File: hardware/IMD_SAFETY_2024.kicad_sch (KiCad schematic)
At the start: 93 parts, among them J1 Main- M80-5300842, K2 TE AXICOM IM07DTS, Q1 2N7002, Q2 2N7002, SW1 Push Button, U1 LM393, U10 74HCS08, U13 74HC74, U14 LM393, U15 LM393, U16 LM393, U2 74AC04SC, U3 74LVC1G79, U6 74LVC1G79, U7 MC78M12CDTG, U8 LM1117IMP-5.0, U9 74HCS32

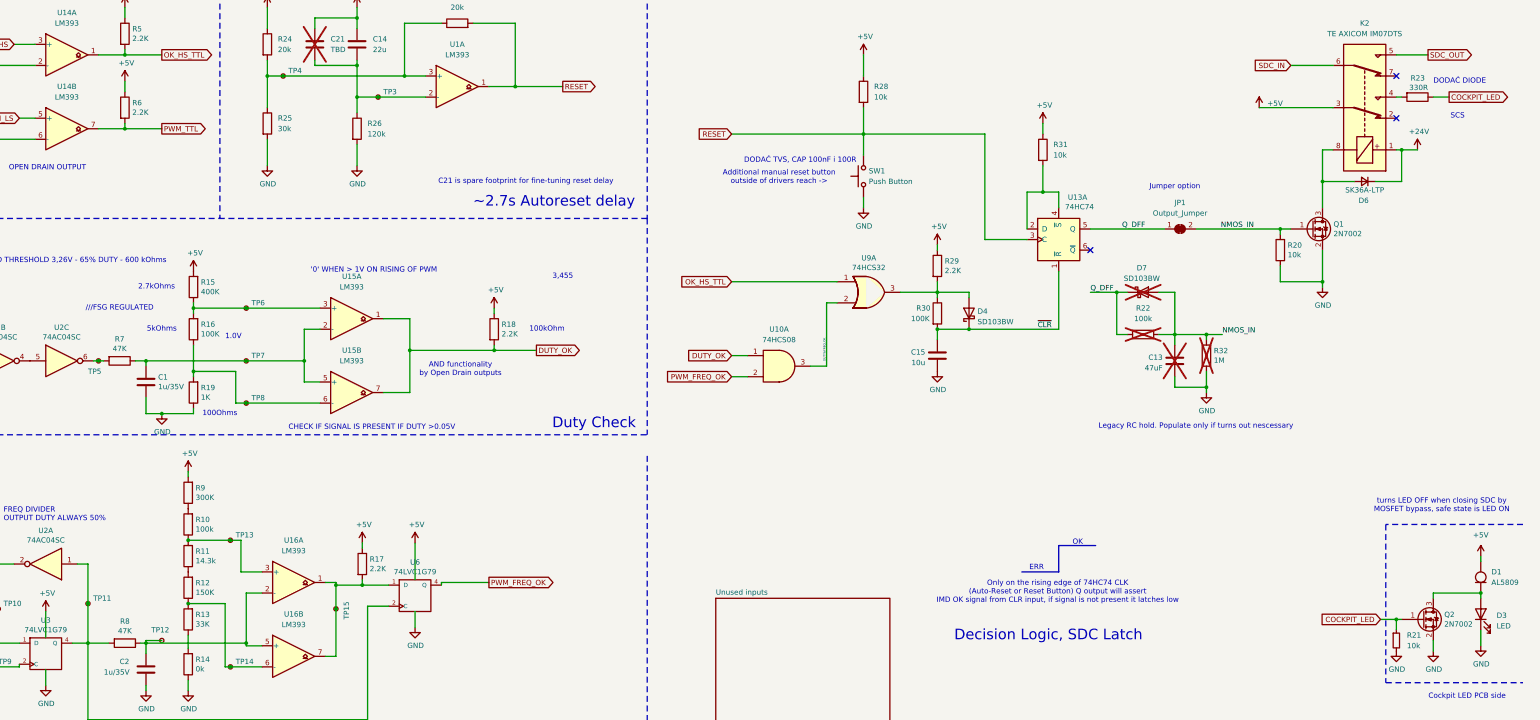
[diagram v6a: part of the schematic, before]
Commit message: Delete legacy RC hold, Add relay diode, Adjust Duty R Values via FSG tweaks TODO: RESET EMI Filter
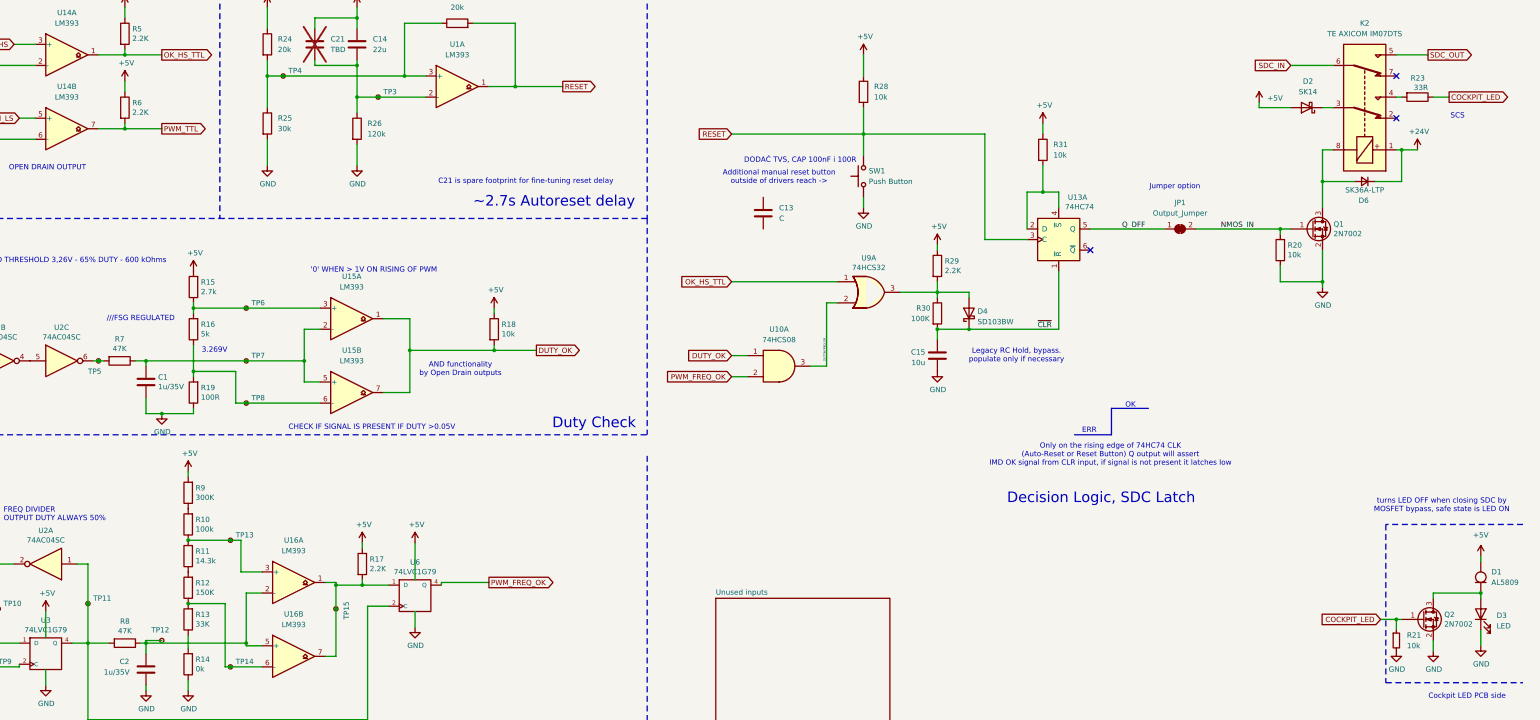
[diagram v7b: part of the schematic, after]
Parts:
- removed C13: 47uF, Capacitor_SMD:C_1206_3216Metric, symbol PUTM_EV_IMD_SAFETY_2021-rescue:C-Device
- removed D7: SD103BW, Diode_SMD:D_SOD-123F, symbol Device:D_Schottky
- removed R22: 100k, Resistor_SMD:R_0603_1608Metric, symbol PUTM_EV_IMD_SAFETY_2021-rescue:R-Device
- removed R32: 1M, Resistor_SMD:R_0603_1608Metric, symbol PUTM_EV_IMD_SAFETY_2021-rescue:R-Device
- added C13: C, symbol Device:C
- added D2: SK14, Diode_SMD:D_SMA, symbol Device:D_Schottky
- R15: value 400K -> 2.7k
- R16: value 100K -> 5k
- R18: value 2.2K -> 10k
- R19: value 1K -> 100R
- R23: value 330R -> 33R; footprint Resistor_SMD:R_0603_1608Metric -> Resistor_SMD:R_0805_2012Metric
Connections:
- net +5V: now also D2.2 (A); no longer K2.3
- new net: D2.1 (K), K2.3
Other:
- note added: "3.269V"
- note added: "Legacy RC Hold, bypass. populate only if necessary"
- note removed: "1.0V"
- note removed: "100Ohms"
- note removed: "100kOhm"
- note removed: "2.7kOhms"
- note removed: "3,455"
- note removed: "5kOhms"
- note removed: "DODAĆ DIODE"
- note removed: "Legacy RC hold. Populate only if turns out nescessary"

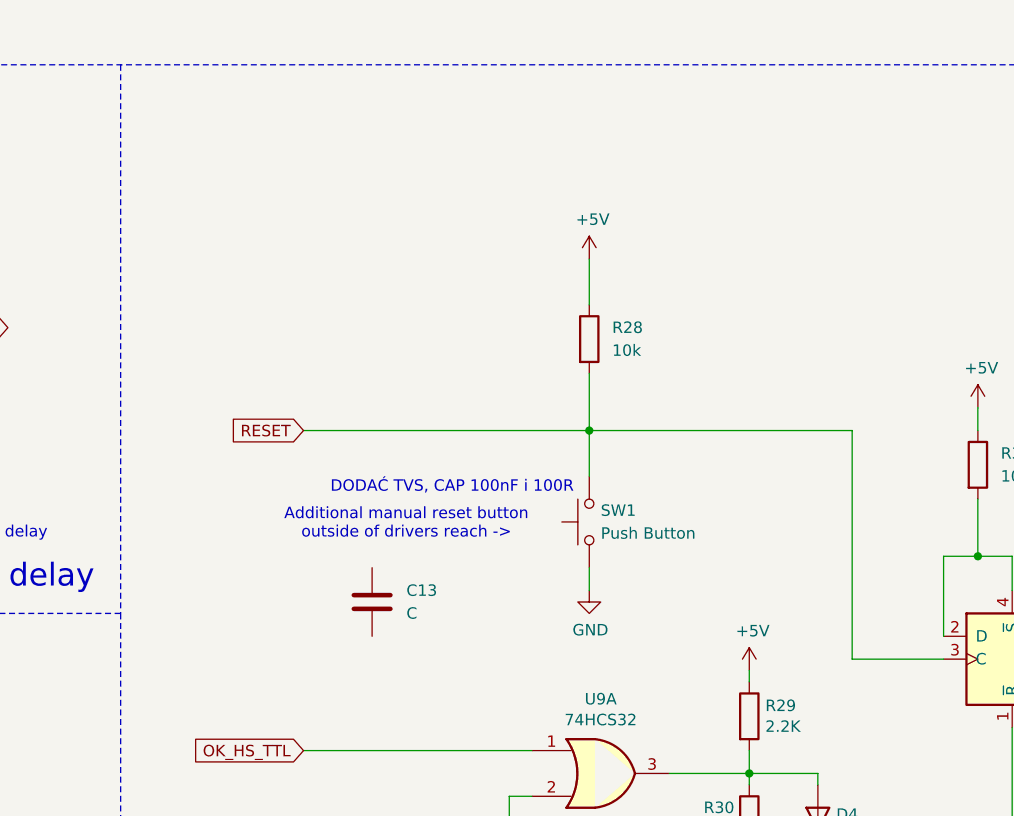
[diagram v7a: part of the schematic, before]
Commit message: Add reset line transient surpression
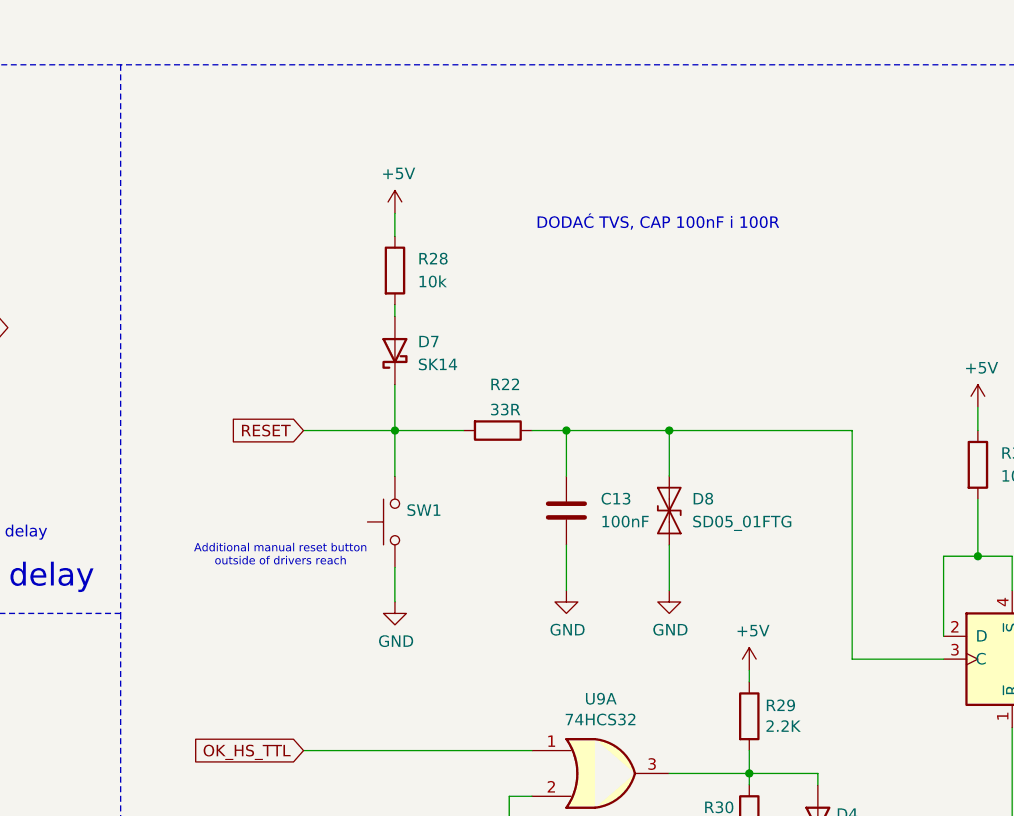
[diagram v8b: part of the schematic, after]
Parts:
- added D7: SK14, Diode_SMD:D_SMA, symbol Device:D_Schottky
- added D8: SD05_01FTG, Diode_SMD:D_SOD-323, symbol Diode:SD05_SOD323
- added R22: 33R, Resistor_SMD:R_0805_2012Metric, symbol PUTM_EV_IMD_SAFETY_2021-rescue:R-Device
- C13: value C -> 100nF; footprint (none) -> Capacitor_SMD:C_0603_1608Metric_Pad1.08x0.95mm_HandSolder
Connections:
- net GND: now also C13.2, D8.2 (A2)
- net RESET: now also D7.1 (K), R22.2; no longer R28.2, U13.3 (C)
- net at C13.1: now also U13.3 (C), D8.1 (A1), R22.1
- new net: D7.2 (A), R28.2
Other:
- note added: "Additional manual reset button outside of drivers reach"
- note removed: "Additional manual reset button outside of drivers reach ->"
- moved on the sheet: C13, R28, SW1
